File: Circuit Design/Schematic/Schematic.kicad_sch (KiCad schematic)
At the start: 26 parts, among them U1 ESP32-WROOM-32

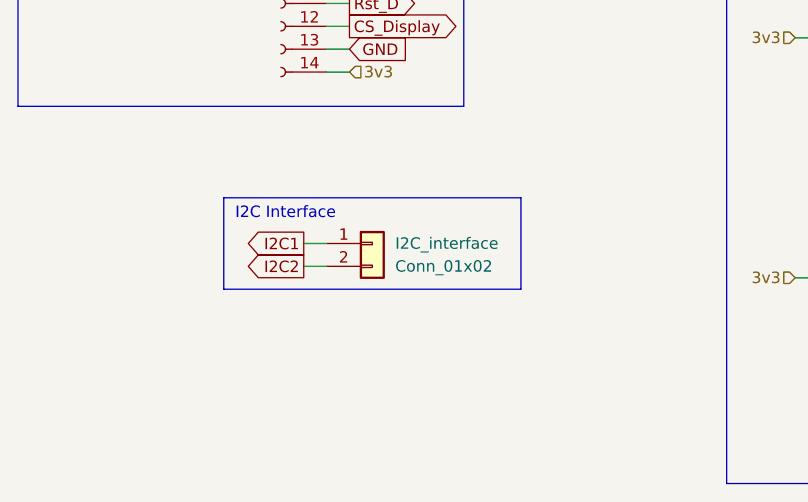
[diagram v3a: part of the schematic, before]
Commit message: Arreglo  I2C
Se ponen junto a la interfaz I2C pines de alimentación que se podrán utilizar según las necesidades observadas
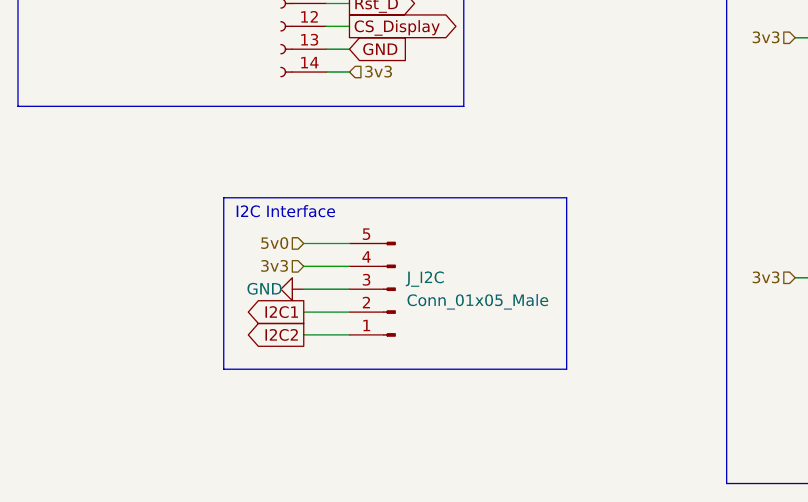
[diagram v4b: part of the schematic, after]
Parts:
- removed I2C_interface: Conn_01x02, Connector_PinSocket_2.54mm:PinSocket_1x02_P2.54mm_Vertical, symbol Connector_Generic:Conn_01x02
- added J_I2C: Conn_01x05_Male, symbol Connector:Conn_01x05_Male
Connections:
- net 3v3: now also J_I2C.4 (Pin_4)
- net 5v0: now also J_I2C.5 (Pin_5)
- net GND: now also J_I2C.3 (Pin_3)
- net I2C1: now also J_I2C.2 (Pin_2)
- net I2C2: now also J_I2C.1 (Pin_1)
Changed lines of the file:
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@@
     (stroke (width 0) (type default) (color 0 0 0 0))
   )
-  (polyline (pts (xy 53.34 163.83) (xy 86.36 163.83))
+  (polyline (pts (xy 53.34 163.83) (xy 91.44 163.83))
     (stroke (width 0) (type default) (color 0 0 0 0))
   )
@@
     (stroke (width 0) (type default) (color 0 0 0 0))
   )
+  (wire (pts (xy 62.23 171.45) (xy 67.31 171.45))
+    (stroke (width 0) (type default) (color 0 0 0 0))
+  )
   (wire (pts (xy 144.78 31.75) (xy 154.94 31.75))
     (stroke (width 0) (type default) (color 0 0 0 0))
@@
     (stroke (width 0) (type default) (color 0 0 0 0))
   )
-  (polyline (pts (xy 86.36 163.83) (xy 86.36 173.99))
+  (polyline (pts (xy 91.44 163.83) (xy 91.44 182.88))
     (stroke (width 0) (type default) (color 0 0 0 0))
   )
@@
     (stroke (width 0) (type default) (color 0 0 0 0))
   )
-  (wire (pts (xy 62.23 171.45) (xy 64.77 171.45))
+  (wire (pts (xy 62.23 179.07) (xy 67.31 179.07))
     (stroke (width 0) (type default) (color 0 0 0 0))
   )
@@
     (stroke (width 0) (type default) (color 0 0 0 0))
   )
-  (wire (pts (xy 62.23 168.91) (xy 64.77 168.91))
+  (wire (pts (xy 62.23 176.53) (xy 67.31 176.53))
     (stroke (width 0) (type default) (color 0 0 0 0))
   )
@@
     (stroke (width 0) (type default) (color 0 0 0 0))
   )
+  (wire (pts (xy 62.23 173.99) (xy 67.31 173.99))
+    (stroke (width 0) (type default) (color 0 0 0 0))
+  )
   (wire (pts (xy 116.84 172.72) (xy 123.19 172.72))
     (stroke (width 0) (type default) (color 0 0 0 0))
@@
     (stroke (width 0) (type default) (color 0 0 0 0))
   )
+  (wire (pts (xy 62.23 168.91) (xy 67.31 168.91))
+    (stroke (width 0) (type default) (color 0 0 0 0))
+  )
   (wire (pts (xy 54.61 46.355) (xy 56.515 46.355))
     (stroke (width 0) (type default) (color 0 0 0 0))
@@
     (stroke (width 0) (type default) (color 0 0 0 0))
   )
-  (polyline (pts (xy 53.34 163.83) (xy 53.34 173.99))
-    (stroke (width 0) (type default) (color 0 0 0 0))
-  )
-  (polyline (pts (xy 86.36 173.99) (xy 53.34 173.99))
+  (polyline (pts (xy 53.34 163.83) (xy 53.34 182.88))
+    (stroke (width 0) (type default) (color 0 0 0 0))
+  )
+  (polyline (pts (xy 91.44 182.88) (xy 53.34 182.88))
     (stroke (width 0) (type default) (color 0 0 0 0))
   )
@@
     )
   )
-  (global_label "I2C2" (shape output) (at 62.23 171.45 180) (fields_autoplaced)
-    (effects (font (size 1.27 1.27)) (justify right))
-    (property "Intersheet References" "${INTERSHEET_REFS}" (id 0) (at 55.612 171.3706 0)
+  (global_label "I2C2" (shape output) (at 62.23 179.07 180) (fields_autoplaced)
+    (effects (font (size 1.27 1.27)) (justify right))
+    (property "Intersheet References" "${INTERSHEET_REFS}" (id 0) (at 55.612 178.9906 0)
       (effects (font (size 1.27 1.27)) (justify right) hide)
     )
@@
     )
   )
-  (global_label "I2C1" (shape output) (at 62.23 168.91 180) (fields_autoplaced)
-    (effects (font (size 1.27 1.27)) (justify right))
-    (property "Intersheet References" "${INTERSHEET_REFS}" (id 0) (at 55.612 168.8306 0)
+  (global_label "I2C1" (shape output) (at 62.23 176.53 180) (fields_autoplaced)
+    (effects (font (size 1.27 1.27)) (justify right))
+    (property "Intersheet References" "${INTERSHEET_REFS}" (id 0) (at 55.612 176.4506 0)
       (effects (font (size 1.27 1.27)) (justify right) hide)
     )
@@
     (effects (font (size 1.27 1.27)) (justify right))
   )
+  (hierarchical_label "5v0" (shape input) (at 62.23 168.91 180)
+    (effects (font (size 1.27 1.27)) (justify right))
+  )
   (hierarchical_label "3v3" (shape input) (at 204.47 109.22 180)
     (effects (font (size 1.27 1.27)) (justify right))
@@
   )
   (hierarchical_label "3v3" (shape input) (at 204.47 161.29 180)
+    (effects (font (size 1.27 1.27)) (justify right))
+  )
+  (hierarchical_label "3v3" (shape input) (at 62.23 171.45 180)
     (effects (font (size 1.27 1.27)) (justify right))
   )
@@
     (pin "4")
   )
-  (symbol (lib_id "Connector_Generic:Conn_01x02") (at 69.85 168.91 0) (unit 1)
-    (in_bom yes) (on_board yes) (fields_autoplaced)
-    (property "Reference" "I2C_interface" (id 0) (at 72.39 168.9099 0)
-      (effects (font (size 1.27 1.27)) (justify left))
-    )
-    (property "Value" "Conn_01x02" (id 1) (at 72.39 171.4499 0)
-      (effects (font (size 1.27 1.27)) (justify left))
-    )
-    (property "Footprint" "Connector_PinSocket_2.54mm:PinSocket_1x02_P2.54mm_Vertical" (id 2) (at 69.85 168.91 0)
-      (effects (font (size 1.27 1.27)) hide)
-    )
-    (property "Datasheet" "~" (id 3) (at 69.85 168.91 0)
-      (effects (font (size 1.27 1.27)) hide)
-    )
-    (pin "1")
-    (pin "2")
-  )
   (symbol (lib_id "power:GND") (at 250.19 121.92 0) (unit 1)
     (in_bom yes) (on_board yes)
@@
     (pin "1")
   )
+  (symbol (lib_id "Connector:Conn_01x05_Male") (at 72.39 173.99 180) (unit 1)
+    (in_bom yes) (on_board yes) (fields_autoplaced)
+    (property "Reference" "J_I2C" (id 0) (at 73.66 172.7199 0)
+      (effects (font (size 1.27 1.27)) (justify right))
+    )
+    (property "Value" "Conn_01x05_Male" (id 1) (at 73.66 175.2599 0)
+      (effects (font (size 1.27 1.27)) (justify right))
+    )
+    (property "Footprint" "" (id 2) (at 72.39 173.99 0)
+      (effects (font (size 1.27 1.27)) hide)
+    )
+    (property "Datasheet" "~" (id 3) (at 72.39 173.99 0)
+      (effects (font (size 1.27 1.27)) hide)
+    )
+    (pin "1")
+    (pin "2")
+    (pin "3")
+    (pin "4")
+    (pin "5")
+  )
   (symbol (lib_id "power:GND") (at 160.02 40.64 0) (unit 1)
     (in_bom yes) (on_board yes)
@@
     (pin "1")
     (pin "2")
+  )
+  (symbol (lib_id "power:GND") (at 62.23 173.99 270) (unit 1)
+    (in_bom yes) (on_board yes)
+    (property "Reference" "#PWR?" (id 0) (at 55.88 173.99 0)
+      (effects (font (size 1.27 1.27)) hide)
+    )
+    (property "Value" "GND" (id 1) (at 55.88 173.99 90)
+      (effects (font (size 1.27 1.27)) (justify left))
+    )
+    (property "Footprint" "" (id 2) (at 62.23 173.99 0)
+      (effects (font (size 1.27 1.27)) hide)
+    )
+    (property "Datasheet" "" (id 3) (at 62.23 173.99 0)
+      (effects (font (size 1.27 1.27)) hide)
+    )
+    (pin "1")
   )
   (symbol (lib_id "power:GND") (at 142.24 160.02 0) (unit 1)
@@
       (reference "#PWR0117") (unit 1) (value "GND") (footprint "")
     )
+    (path "/e0b6636f-62b9-430c-a8cd-ac04e092cfb7"
+      (reference "#PWR?") (unit 1) (value "GND") (footprint "")
+    )
     (path "/95a18f92-c1c4-48fb-be0b-427e95ae1db4"
       (reference "Button_Damage") (unit 1) (value "SW_DIP_x05") (footprint "")
@@
       (reference "ESP_Reset") (unit 1) (value "SW_DIP_x01") (footprint "")
     )
-    (path "/567b521c-82db-4d61-8d43-df73e3cabec5"
-      (reference "I2C_interface") (unit 1) (value "Conn_01x02") (footprint "Connector_PinSocket_2.54mm:PinSocket_1x02_P2.54mm_Vertical")
+    (path "/bcb4603d-3b74-4899-88d5-9691245cae1c"
+      (reference "J_I2C") (unit 1) (value "Conn_01x05_Male") (footprint "")
     )
     (path "/a45a8d32-ecf4-4f16-b72c-3f69eaa16341"
